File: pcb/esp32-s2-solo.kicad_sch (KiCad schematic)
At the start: 8 parts, among them U2 ESP32-S2-SOLO

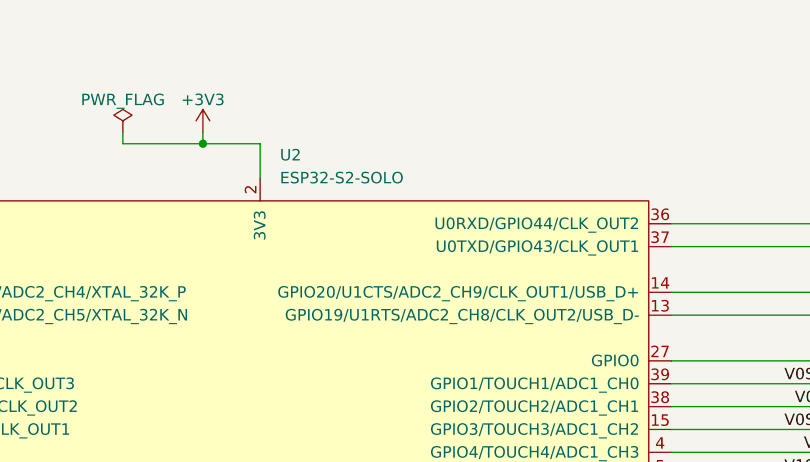
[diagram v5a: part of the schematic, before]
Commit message: Ignored thermal-relief + changed ESP32-S2 to be ESP32-S3-N8
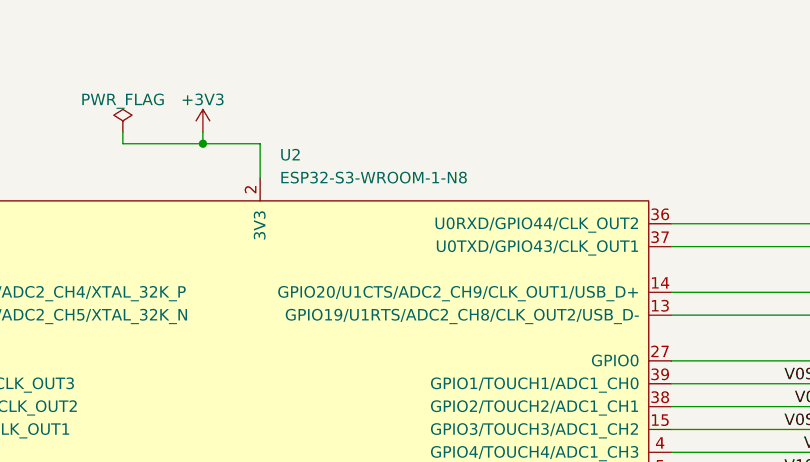
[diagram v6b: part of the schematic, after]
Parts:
- U2: value ESP32-S2-SOLO -> ESP32-S3-WROOM-1-N8
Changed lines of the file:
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@@
       (effects (font (size 1.27 1.27)) (justify left))
     )
-    (property "Value" "ESP32-S2-SOLO" (at 209.2041 30.48 0)
+    (property "Value" "ESP32-S3-WROOM-1-N8" (at 209.2041 30.48 0)
       (effects (font (size 1.27 1.27)) (justify left))
     )
